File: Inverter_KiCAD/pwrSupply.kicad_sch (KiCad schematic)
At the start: 7 parts, among them J1 PX0580-PC-12132, J2 173010542, U11 AZ1117-3.3, U4 MP-LD30-23B12R2

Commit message: assigments footprints
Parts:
- removed J2: 173010542, CONN3_10542_WRE, symbol 173010578:173010542
- added U17: 173010542, Custom:173010578, symbol 173010578:173010542
- C31: renamed from C22; footprint (none) -> Capacitor_SMD:CP_Elec_4x5.4; MFR (none) -> 865060440001
- C32: renamed from C23; footprint (none) -> Capacitor_SMD:CP_Elec_5x5.4; MFR (none) -> 865060442002
- F1: footprint (none) -> Fuse:Fuseholder_Clip-5x20mm_Bel_FC-203-22_Lateral_P17.80x5.00mm_D1.17mm_Horizontal
- J1: footprint CONN_PX0580/PC/12132_BUL -> Custom:PX0580-PC-12132
- U13: renamed from U4; footprint MP-LD30-23BXXR2_MTC -> MP-LD30-23B15R2:MP-LD30-23B15R2
- U14: renamed from U11; footprint (none) -> Package_TO_SOT_SMD:SOT-223-3_TabPin2
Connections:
- net ISO_15V: now also U17.1 (VIN)
- net ISO_5V: now also U17.3 (5V)
- net ISO_GND: now also U17.2 (GND)

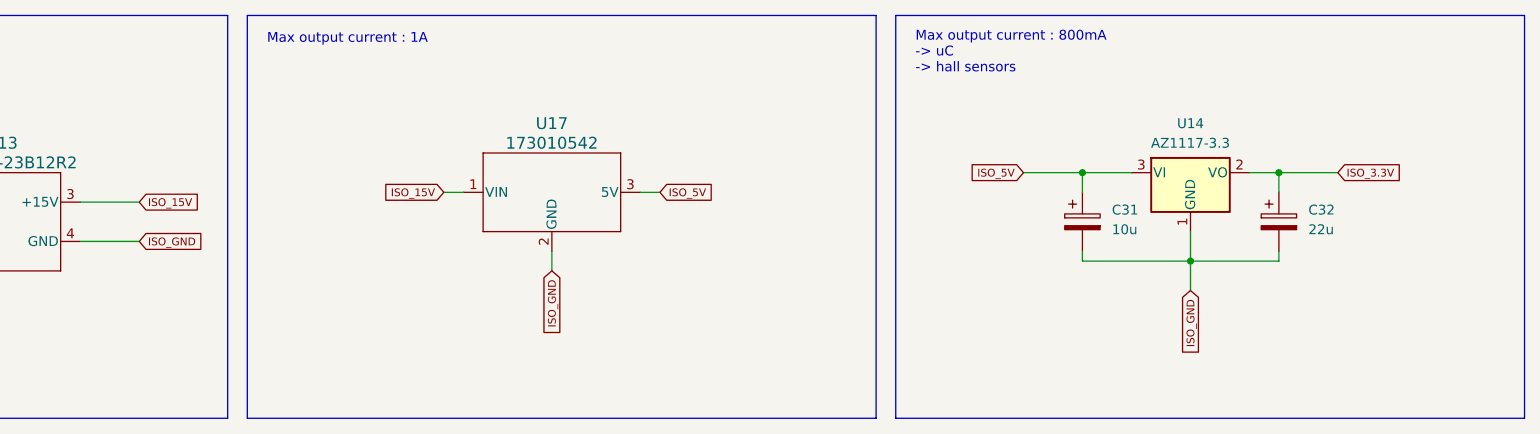
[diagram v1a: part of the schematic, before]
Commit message: update schematic
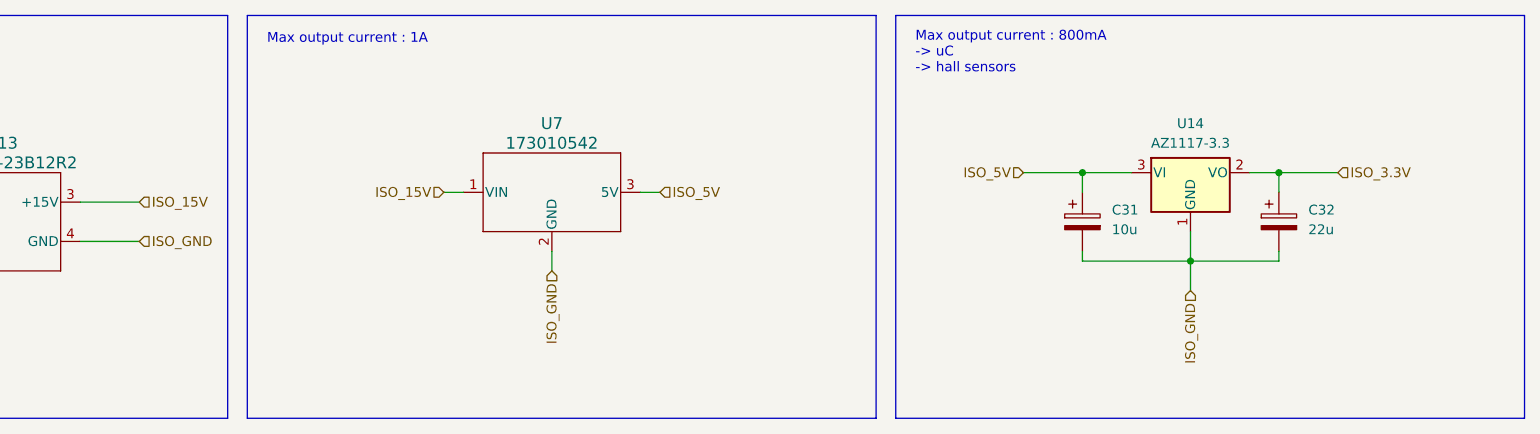
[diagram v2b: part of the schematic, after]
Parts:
- removed U17: 173010542, Custom:173010578, symbol 173010578:173010542
- added U7: 173010542, symbol Custom:173010542
- F1: footprint Fuse:Fuseholder_Clip-5x20mm_Bel_FC-203-22_Lateral_P17.80x5.00mm_D1.17mm_Horizontal -> (none)
- U13: footprint MP-LD30-23B15R2:MP-LD30-23B15R2 -> Custom:MP-LD30-23B15R2
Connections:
- net ISO_15V: now also U7.1 (VIN)
- net ISO_5V: now also U7.3 (5V)
- net ISO_GND: now also U7.2 (GND)
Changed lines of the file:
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@@
     (effects (font (size 1.27 1.27)) (justify left bottom))
   )
-  (global_label "ISO_GND" (shape input) (at 83.82 43.18 0) (fields_autoplaced)
-    (effects (font (size 1 1)) (justify left))
-    (property "Intersheetrefs" "${INTERSHEET_REFS}" (at 92.3936 43.18 0)
-      (effects (font (size 1.27 1.27)) (justify left) hide)
-    )
-  )
-  (global_label "ISO_GND" (shape input) (at 137.16 46.99 270) (fields_autoplaced)
-    (effects (font (size 1 1)) (justify right))
-    (property "Intersheetrefs" "${INTERSHEET_REFS}" (at 137.16 55.5636 90)
-      (effects (font (size 1.27 1.27)) (justify right) hide)
-    )
-  )
-  (global_label "ISO_3.3V" (shape input) (at 238.76 34.29 0) (fields_autoplaced)
-    (effects (font (size 1 1)) (justify left))
-    (property "Intersheetrefs" "${INTERSHEET_REFS}" (at 247.5241 34.29 0)
-      (effects (font (size 1.27 1.27)) (justify left) hide)
-    )
-  )
-  (global_label "ISO_15V" (shape input) (at 123.19 36.83 180) (fields_autoplaced)
-    (effects (font (size 1 1)) (justify right))
-    (property "Intersheetrefs" "${INTERSHEET_REFS}" (at 114.9021 36.83 0)
-      (effects (font (size 1.27 1.27)) (justify right) hide)
-    )
-  )
-  (global_label "ISO_GND" (shape input) (at 219.71 49.53 270) (fields_autoplaced)
-    (effects (font (size 1 1)) (justify right))
-    (property "Intersheetrefs" "${INTERSHEET_REFS}" (at 219.71 58.1036 90)
-      (effects (font (size 1.27 1.27)) (justify right) hide)
-    )
-  )
-  (global_label "ISO_5V" (shape input) (at 151.13 36.83 0) (fields_autoplaced)
-    (effects (font (size 1 1)) (justify left))
-    (property "Intersheetrefs" "${INTERSHEET_REFS}" (at 158.4655 36.83 0)
-      (effects (font (size 1.27 1.27)) (justify left) hide)
-    )
-  )
-  (global_label "ISO_5V" (shape input) (at 198.12 34.29 180) (fields_autoplaced)
-    (effects (font (size 1 1)) (justify right))
-    (property "Intersheetrefs" "${INTERSHEET_REFS}" (at 190.7845 34.29 0)
-      (effects (font (size 1.27 1.27)) (justify right) hide)
-    )
-  )
-  (global_label "ISO_15V" (shape input) (at 83.82 38.1 0) (fields_autoplaced)
-    (effects (font (size 1 1)) (justify left))
-    (property "Intersheetrefs" "${INTERSHEET_REFS}" (at 92.1079 38.1 0)
-      (effects (font (size 1.27 1.27)) (justify left) hide)
-    )
+  (hierarchical_label "ISO_3.3V" (shape input) (at 238.76 34.29 0) (fields_autoplaced)
+    (effects (font (size 1.27 1.27)) (justify left))
+  )
+  (hierarchical_label "ISO_5V" (shape input) (at 151.13 36.83 0) (fields_autoplaced)
+    (effects (font (size 1.27 1.27)) (justify left))
+  )
+  (hierarchical_label "ISO_15V" (shape input) (at 123.19 36.83 180) (fields_autoplaced)
+    (effects (font (size 1.27 1.27)) (justify right))
+  )
+  (hierarchical_label "ISO_15V" (shape input) (at 83.82 38.1 0) (fields_autoplaced)
+    (effects (font (size 1.27 1.27)) (justify left))
+  )
+  (hierarchical_label "ISO_GND" (shape input) (at 83.82 43.18 0) (fields_autoplaced)
+    (effects (font (size 1.27 1.27)) (justify left))
+  )
+  (hierarchical_label "ISO_GND" (shape input) (at 137.16 46.99 270) (fields_autoplaced)
+    (effects (font (size 1.27 1.27)) (justify right))
+  )
+  (hierarchical_label "ISO_5V" (shape input) (at 198.12 34.29 180) (fields_autoplaced)
+    (effects (font (size 1.27 1.27)) (justify right))
+  )
+  (hierarchical_label "ISO_GND" (shape input) (at 219.71 49.53 270) (fields_autoplaced)
+    (effects (font (size 1.27 1.27)) (justify right))
   )
   (symbol (lib_id "power:Earth") (at 35.56 40.64 90) (unit 1)
@@
       (effects (font (size 1.27 1.27)))
     )
-    (property "Footprint" "Fuse:Fuseholder_Clip-5x20mm_Bel_FC-203-22_Lateral_P17.80x5.00mm_D1.17mm_Horizontal" (at 45.72 44.958 90)
+    (property "Footprint" "" (at 45.72 44.958 90)
       (effects (font (size 1.27 1.27)) hide)
     )
@@
     )
   )
+  (symbol (lib_id "Custom:173010542") (at 137.16 36.83 0) (unit 1)
+    (in_bom yes) (on_board yes) (dnp no) (fields_autoplaced)
+    (property "Reference" "U7" (at 137.16 27.94 0)
+      (effects (font (size 1.524 1.524)))
+    )
+    (property "Value" "173010542" (at 137.16 30.48 0)
+      (effects (font (size 1.524 1.524)))
+    )
+    (property "Footprint" "" (at 149.86 49.53 0)
+      (effects (font (size 1.27 1.27) italic) hide)
+    )
+    (property "Datasheet" "173010542" (at 147.32 46.99 0)
+      (effects (font (size 1.27 1.27) italic) hide)
+    )
+    (pin "1")
+    (pin "2")
+    (pin "3")
+    (instances
+      (project "Inverter_KiCAD"
+        (path "/5e6c1e3f-0815-454a-8acb-8e3e2d064875/0406dcca-4785-4175-98fc-8c562936c28c"
+          (reference "U7") (unit 1)
+        )
+      )
+    )
+  )
   (symbol (lib_id "Device:C_Polarized") (at 205.74 40.64 0) (unit 1)
     (in_bom yes) (on_board yes) (dnp no) (fields_autoplaced)
@@
       (effects (font (size 1.524 1.524)))
     )
-    (property "Footprint" "MP-LD30-23B15R2:MP-LD30-23B15R2" (at 71.12 53.34 0)
+    (property "Footprint" "Custom:MP-LD30-23B15R2" (at 71.12 53.34 0)
       (effects (font (size 1.27 1.27) italic) hide)
     )
@@
         )
       )
-    )
-  )
-  (symbol (lib_id "173010578:173010542") (at 137.16 36.83 0) (unit 1)
-    (in_bom yes) (on_board yes) (dnp no) (fields_autoplaced)
-    (property "Reference" "U17" (at 137.16 27.94 0)
-      (effects (font (size 1.524 1.524)))
-    )
-    (property "Value" "173010542" (at 137.16 30.48 0)
-      (effects (font (size 1.524 1.524)))
-    )
-    (property "Footprint" "Custom:173010578" (at 149.86 49.53 0)
-      (effects (font (size 1.27 1.27) italic) hide)
-    )
-    (property "Datasheet" "173010542" (at 147.32 46.99 0)
-      (effects (font (size 1.27 1.27) italic) hide)
-    )
-    (pin "1")
-    (pin "2")
-    (pin "3")
-    (instances
-      (project "Inverter_KiCAD"
-        (path "/5e6c1e3f-0815-454a-8acb-8e3e2d064875/0406dcca-4785-4175-98fc-8c562936c28c"
-          (reference "U17") (unit 1)
-        )
-      )

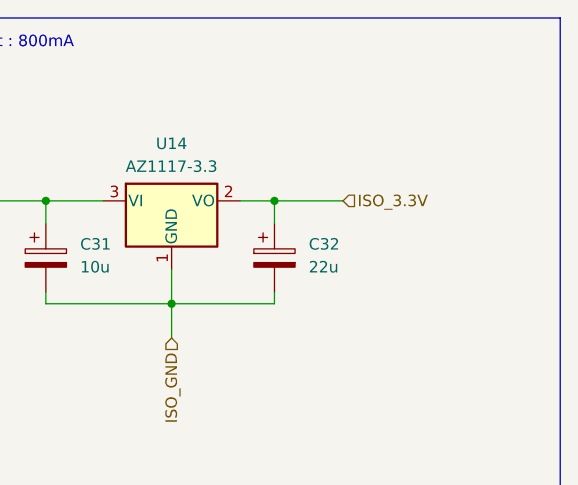
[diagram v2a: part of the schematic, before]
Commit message: update schematic
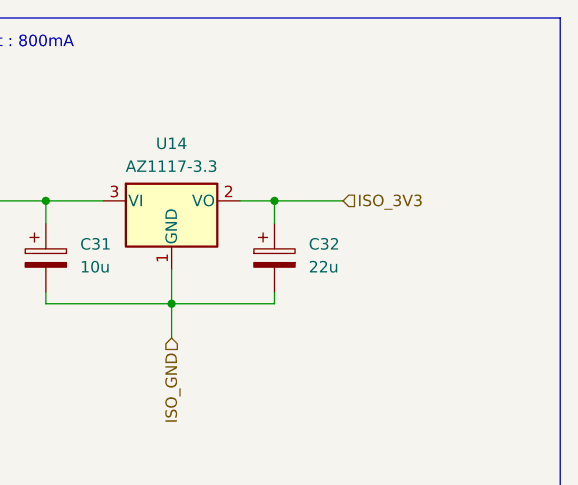
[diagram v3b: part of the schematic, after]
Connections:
- net ISO_3.3V renamed ISO_3V3
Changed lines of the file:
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@@
     (effects (font (size 1.27 1.27)) (justify left bottom))
   )
-  (hierarchical_label "ISO_3.3V" (shape input) (at 238.76 34.29 0) (fields_autoplaced)
+  (hierarchical_label "ISO_3V3" (shape input) (at 238.76 34.29 0) (fields_autoplaced)
     (effects (font (size 1.27 1.27)) (justify left))
   )

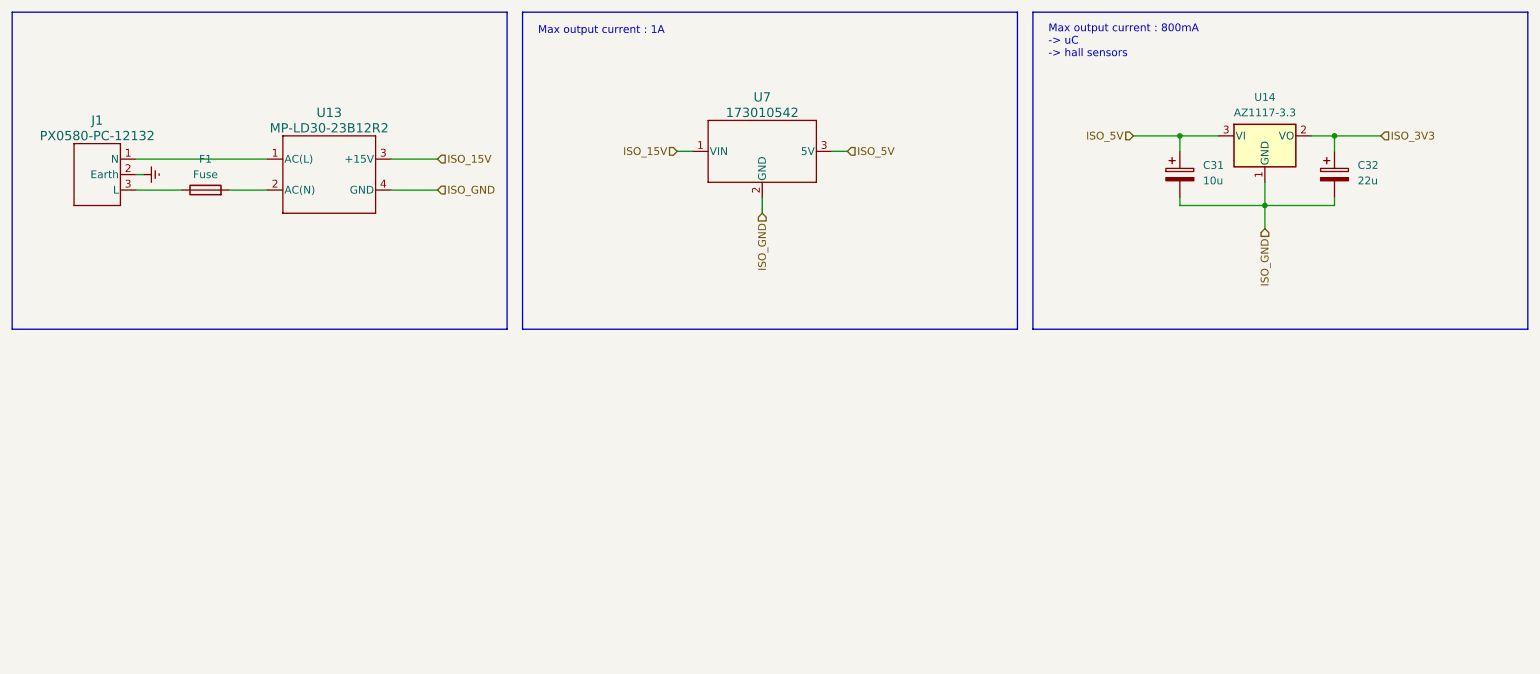
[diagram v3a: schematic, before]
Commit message: clear schematic errors
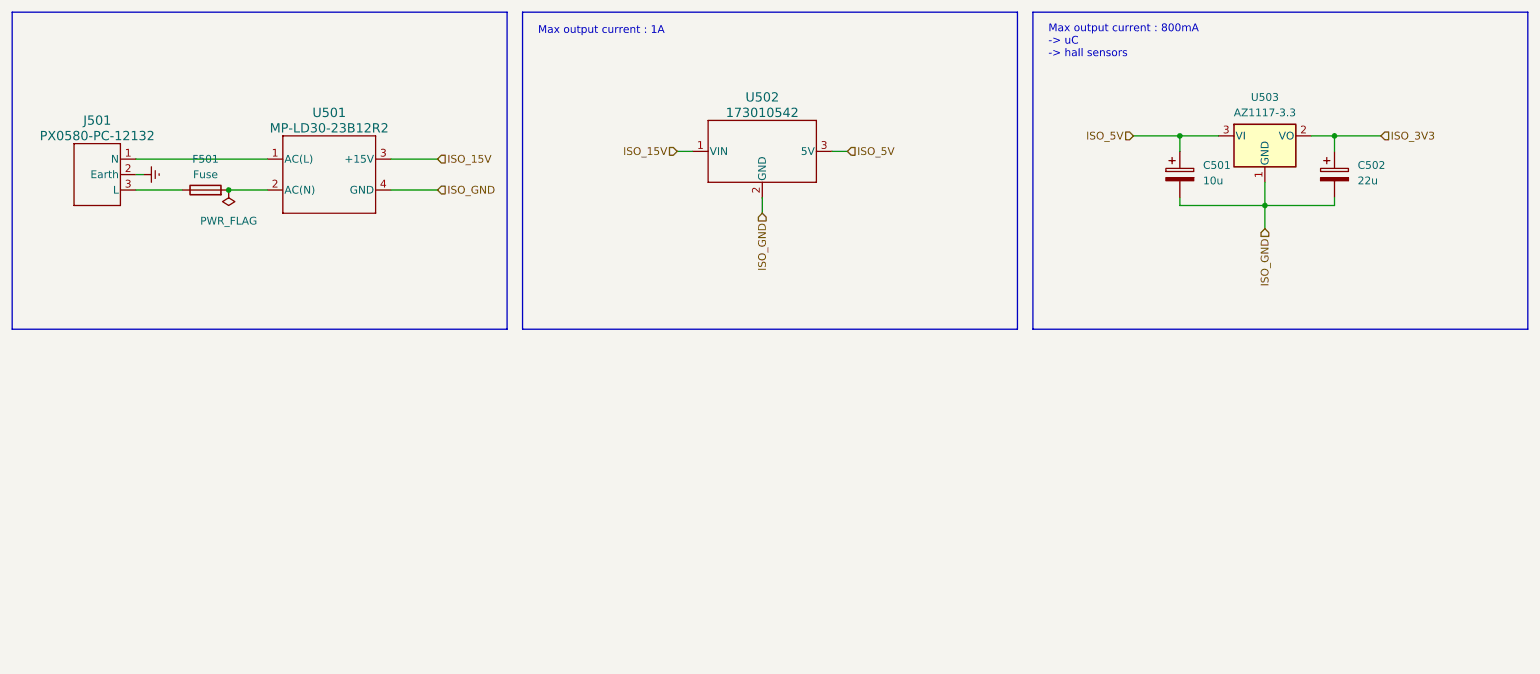
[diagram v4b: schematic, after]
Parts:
- renumbered C31 to C501, C32 to C502, F1 to F501, J1 to J501, U13 to U501, U7 to U502, U14 to U503
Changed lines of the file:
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@@
   (junction (at 219.71 45.72) (diameter 0) (color 0 0 0 0)
   )
+  (junction (at 49.53 43.18) (diameter 0) (color 0 0 0 0)
+  )
   (junction (at 205.74 34.29) (diameter 0) (color 0 0 0 0)
   )
@@
     (stroke (width 0) (type default))
   )
+  (wire (pts (xy 219.71 45.72) (xy 219.71 41.91))
+    (stroke (width 0) (type default))
+  )
+  (wire (pts (xy 34.29 40.64) (xy 35.56 40.64))
+    (stroke (width 0) (type default))
+  )
+  (wire (pts (xy 231.14 44.45) (xy 231.14 45.72))
+    (stroke (width 0) (type default))
+  )
+  (wire (pts (xy 137.16 46.99) (xy 137.16 44.45))
+    (stroke (width 0) (type default))
+  )
+  (wire (pts (xy 219.71 49.53) (xy 219.71 45.72))
+    (stroke (width 0) (type default))
+  )
+  (wire (pts (xy 205.74 34.29) (xy 212.09 34.29))
+    (stroke (width 0) (type default))
+  )
   (wire (pts (xy 34.29 38.1) (xy 55.88 38.1))
-    (stroke (width 0) (type default))
-  )
-  (wire (pts (xy 219.71 45.72) (xy 219.71 41.91))
-    (stroke (width 0) (type default))
-  )
-  (wire (pts (xy 34.29 40.64) (xy 35.56 40.64))
-    (stroke (width 0) (type default))
-  )
-  (wire (pts (xy 231.14 44.45) (xy 231.14 45.72))
-    (stroke (width 0) (type default))
-  )
-  (wire (pts (xy 137.16 46.99) (xy 137.16 44.45))
-    (stroke (width 0) (type default))
-  )
-  (wire (pts (xy 219.71 49.53) (xy 219.71 45.72))
-    (stroke (width 0) (type default))
-  )
-  (wire (pts (xy 205.74 34.29) (xy 212.09 34.29))
     (stroke (width 0) (type default))
   )
@@
   (symbol (lib_id "power:Earth") (at 35.56 40.64 90) (unit 1)
     (in_bom yes) (on_board yes) (dnp no) (fields_autoplaced)
-    (property "Reference" "#PWR031" (at 41.91 40.64 0)
+    (property "Reference" "#PWR0501" (at 41.91 40.64 0)
       (effects (font (size 1.27 1.27)) hide)
     )
@@
       (project "Inverter_KiCAD"
         (path "/5e6c1e3f-0815-454a-8acb-8e3e2d064875/0406dcca-4785-4175-98fc-8c562936c28c"
-          (reference "#PWR031") (unit 1)
+          (reference "#PWR0501") (unit 1)
         )
       )
@@
   (symbol (lib_id "Device:C_Polarized") (at 231.14 40.64 0) (unit 1)
     (in_bom yes) (on_board yes) (dnp no) (fields_autoplaced)
-    (property "Reference" "C32" (at 234.95 39.116 0)
+    (property "Reference" "C502" (at 234.95 39.116 0)
       (effects (font (size 1.27 1.27)) (justify left))
     )
@@
       (project "Inverter_KiCAD"
         (path "/5e6c1e3f-0815-454a-8acb-8e3e2d064875/0406dcca-4785-4175-98fc-8c562936c28c"
-          (reference "C32") (unit 1)
+          (reference "C502") (unit 1)
         )
       )
@@
   (symbol (lib_id "Regulator_Linear:AZ1117-3.3") (at 219.71 34.29 0) (unit 1)
     (in_bom yes) (on_board yes) (dnp no) (fields_autoplaced)
-    (property "Reference" "U14" (at 219.71 27.94 0)
+    (property "Reference" "U503" (at 219.71 27.94 0)
       (effects (font (size 1.27 1.27)))
     )
@@
       (project "Inverter_KiCAD"
         (path "/5e6c1e3f-0815-454a-8acb-8e3e2d064875/0406dcca-4785-4175-98fc-8c562936c28c"
-          (reference "U14") (unit 1)
+          (reference "U503") (unit 1)
         )
       )
@@
   (symbol (lib_id "PX0580-PC-12132:PX0580-PC-12132") (at 31.75 40.64 0) (unit 1)
     (in_bom yes) (on_board yes) (dnp no) (fields_autoplaced)
-    (property "Reference" "J1" (at 27.94 31.75 0)
+    (property "Reference" "J501" (at 27.94 31.75 0)
       (effects (font (size 1.524 1.524)))
     )
@@
       (project "Inverter_KiCAD"
         (path "/5e6c1e3f-0815-454a-8acb-8e3e2d064875/0406dcca-4785-4175-98fc-8c562936c28c"
-          (reference "J1") (unit 1)
+          (reference "J501") (unit 1)
+        )
+      )
+    )
+  )
+  (symbol (lib_id "power:PWR_FLAG") (at 49.53 43.18 180) (unit 1)
+    (in_bom yes) (on_board yes) (dnp no) (fields_autoplaced)
+    (property "Reference" "#FLG0501" (at 49.53 45.085 0)
+      (effects (font (size 1.27 1.27)) hide)
+    )
+    (property "Value" "PWR_FLAG" (at 49.53 48.26 0)
+      (effects (font (size 1.27 1.27)))
+    )
+    (property "Footprint" "" (at 49.53 43.18 0)
+      (effects (font (size 1.27 1.27)) hide)
+    )
+    (property "Datasheet" "~" (at 49.53 43.18 0)
+      (effects (font (size 1.27 1.27)) hide)
+    )
+    (pin "1")
+    (instances
+      (project "Inverter_KiCAD"
+        (path "/5e6c1e3f-0815-454a-8acb-8e3e2d064875/0406dcca-4785-4175-98fc-8c562936c28c"
+          (reference "#FLG0501") (unit 1)
         )
       )
@@
   (symbol (lib_id "Device:Fuse") (at 45.72 43.18 90) (unit 1)
     (in_bom yes) (on_board yes) (dnp no) (fields_autoplaced)
-    (property "Reference" "F1" (at 45.72 38.1 90)
+    (property "Reference" "F501" (at 45.72 38.1 90)
       (effects (font (size 1.27 1.27)))
     )
@@
       (project "Inverter_KiCAD"
         (path "/5e6c1e3f-0815-454a-8acb-8e3e2d064875/0406dcca-4785-4175-98fc-8c562936c28c"
-          (reference "F1") (unit 1)
+          (reference "F501") (unit 1)
         )
       )
@@
   (symbol (lib_id "Custom:173010542") (at 137.16 36.83 0) (unit 1)
     (in_bom yes) (on_board yes) (dnp no) (fields_autoplaced)
-    (property "Reference" "U7" (at 137.16 27.94 0)
+    (property "Reference" "U502" (at 137.16 27.94 0)
       (effects (font (size 1.524 1.524)))
     )
@@
       (project "Inverter_KiCAD"
         (path "/5e6c1e3f-0815-454a-8acb-8e3e2d064875/0406dcca-4785-4175-98fc-8c562936c28c"
-          (reference "U7") (unit 1)
+          (reference "U502") (unit 1)
         )
       )
@@
   (symbol (lib_id "Device:C_Polarized") (at 205.74 40.64 0) (unit 1)
     (in_bom yes) (on_board yes) (dnp no) (fields_autoplaced)
-    (property "Reference" "C31" (at 209.55 39.116 0)
+    (property "Reference" "C501" (at 209.55 39.116 0)
       (effects (font (size 1.27 1.27)) (justify left))
     )
@@
       (project "Inverter_KiCAD"
         (path "/5e6c1e3f-0815-454a-8acb-8e3e2d064875/0406dcca-4785-4175-98fc-8c562936c28c"
-          (reference "C31") (unit 1)
+          (reference "C501") (unit 1)
         )
       )
@@
   (symbol (lib_id "MP-LD30-23B15R2:MP-LD30-23B12R2") (at 66.04 40.64 0) (unit 1)
     (in_bom yes) (on_board yes) (dnp no) (fields_autoplaced)
-    (property "Reference" "U13" (at 66.04 30.48 0)
+    (property "Reference" "U501" (at 66.04 30.48 0)
       (effects (font (size 1.524 1.524)))
     )
@@
       (project "Inverter_KiCAD"
         (path "/5e6c1e3f-0815-454a-8acb-8e3e2d064875/0406dcca-4785-4175-98fc-8c562936c28c"
-          (reference "U13") (unit 1)
-        )
-      )
+          (reference "U501") (unit 1)
+        )
+      )
